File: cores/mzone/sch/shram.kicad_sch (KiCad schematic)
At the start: 10 parts

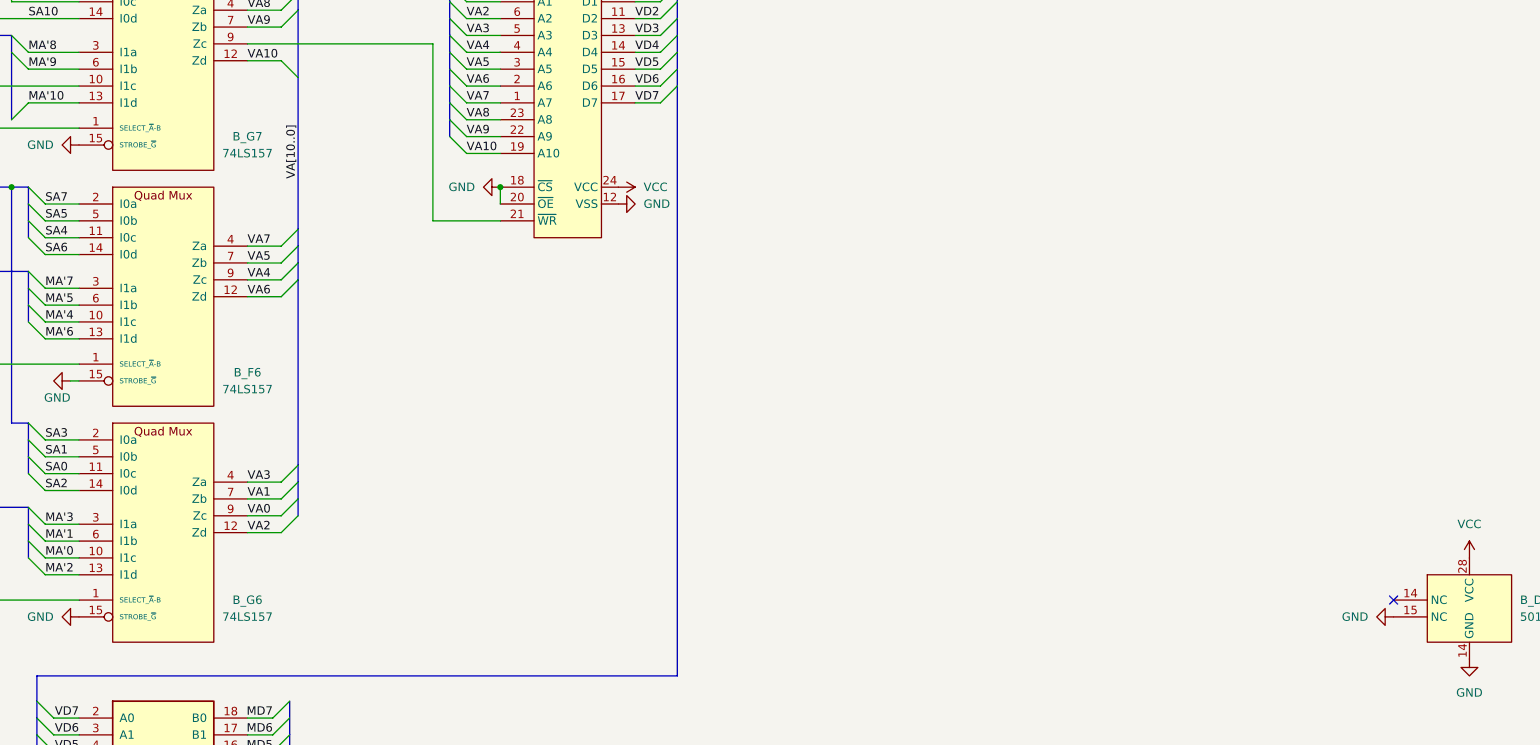
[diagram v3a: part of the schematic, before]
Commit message: mzone core
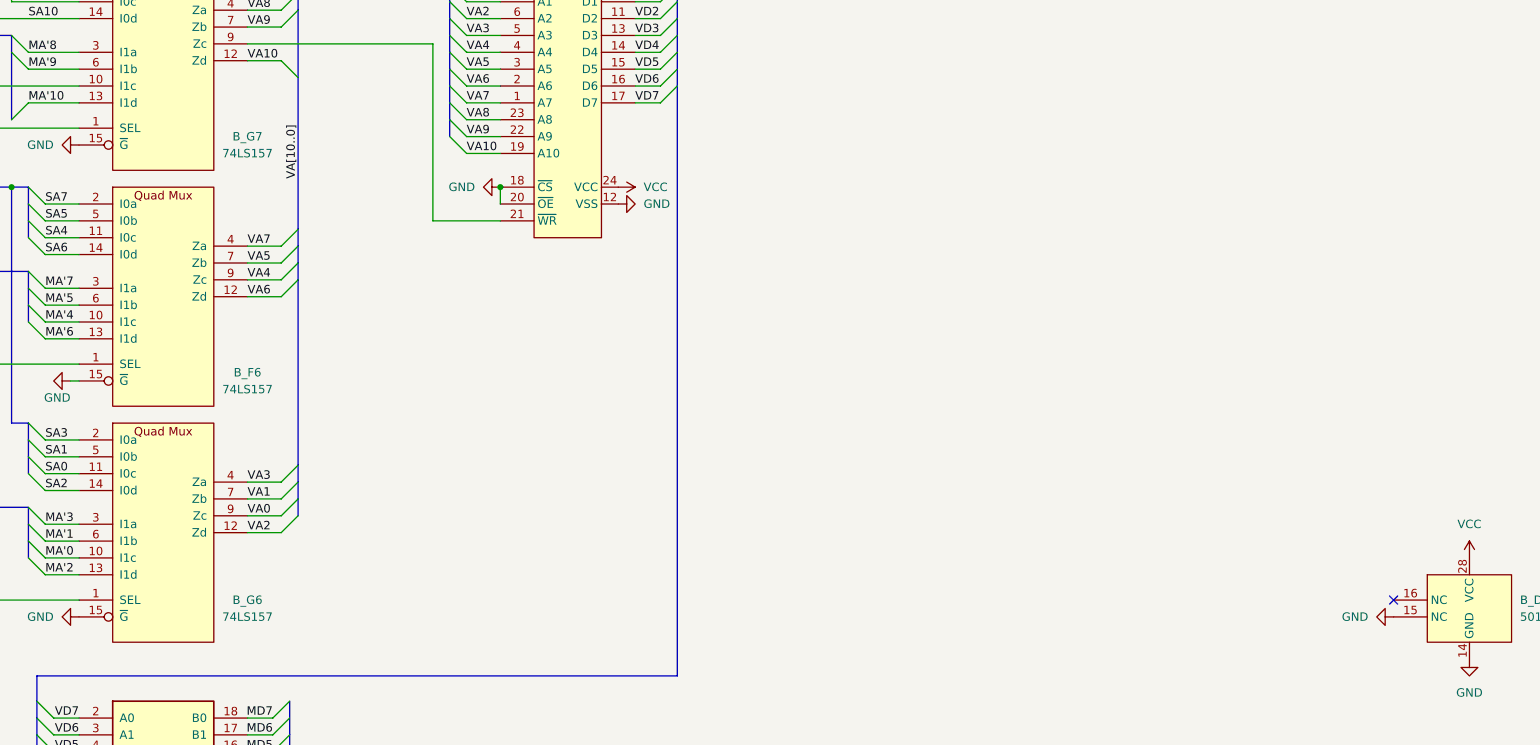
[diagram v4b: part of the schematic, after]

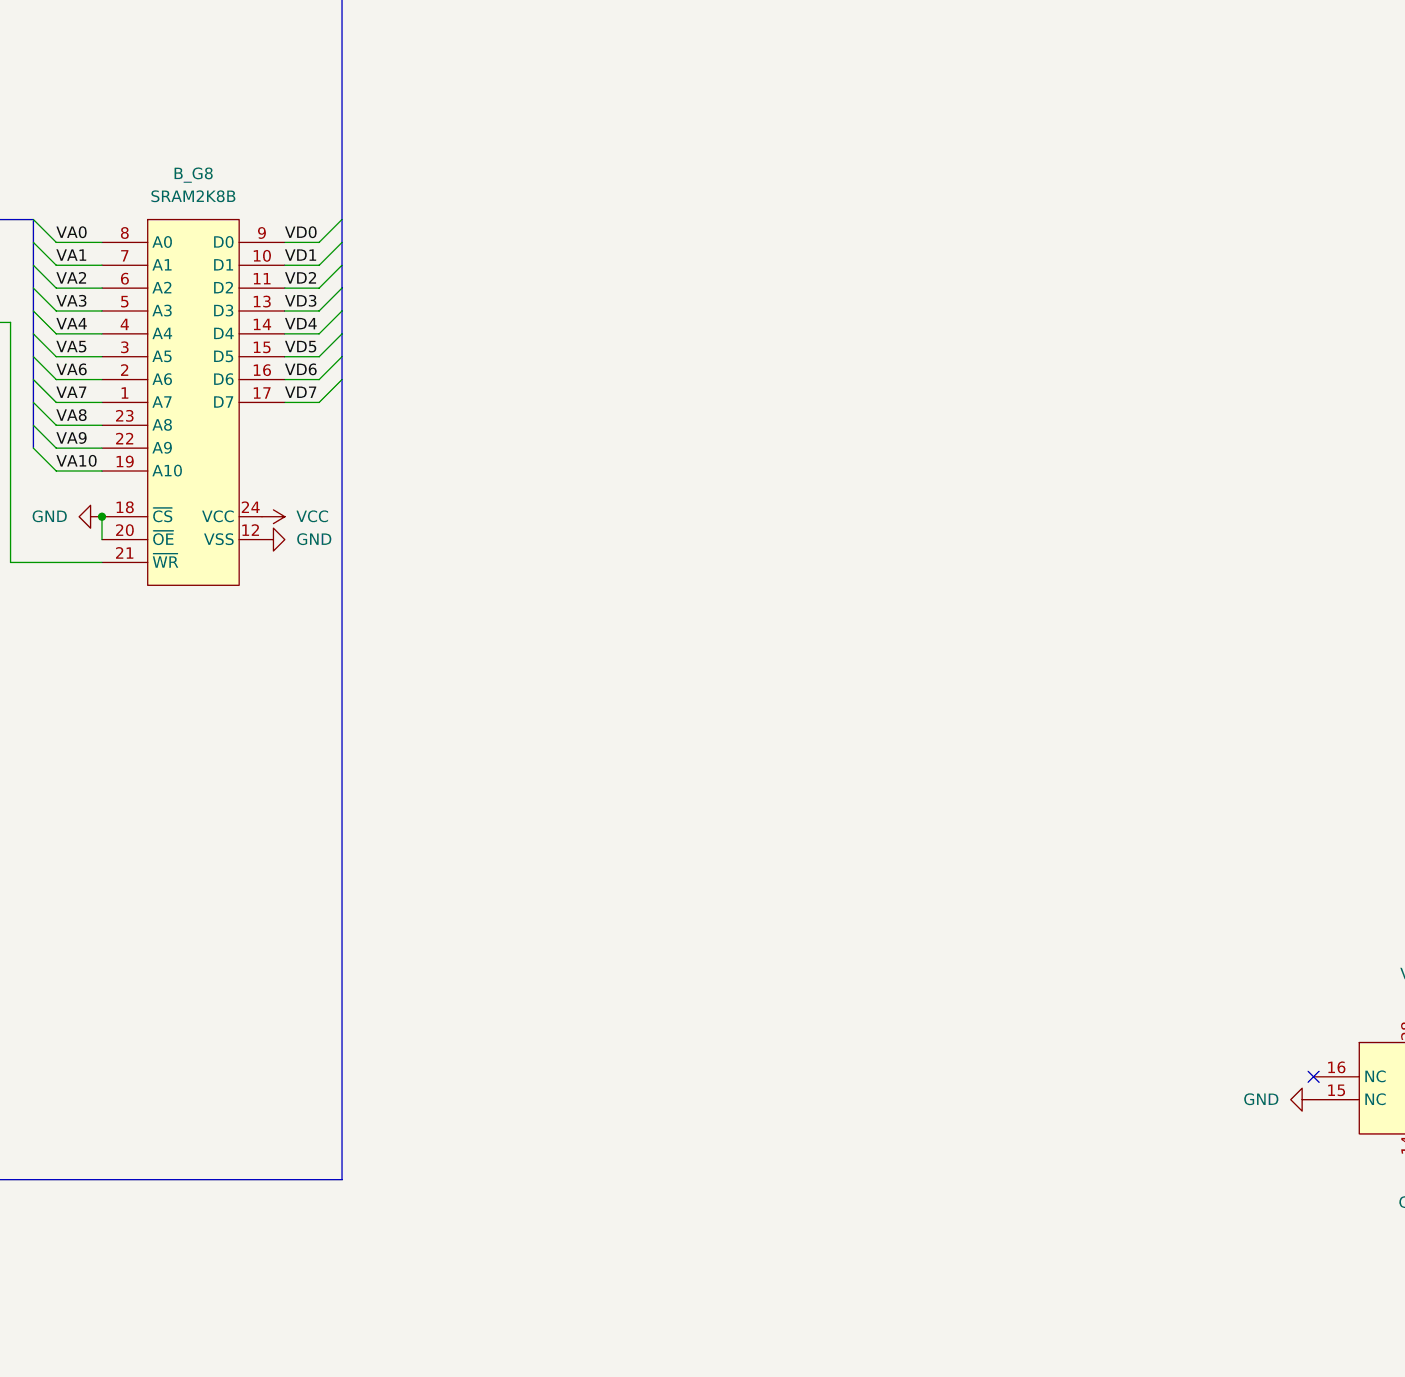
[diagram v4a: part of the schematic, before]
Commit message: mzone core
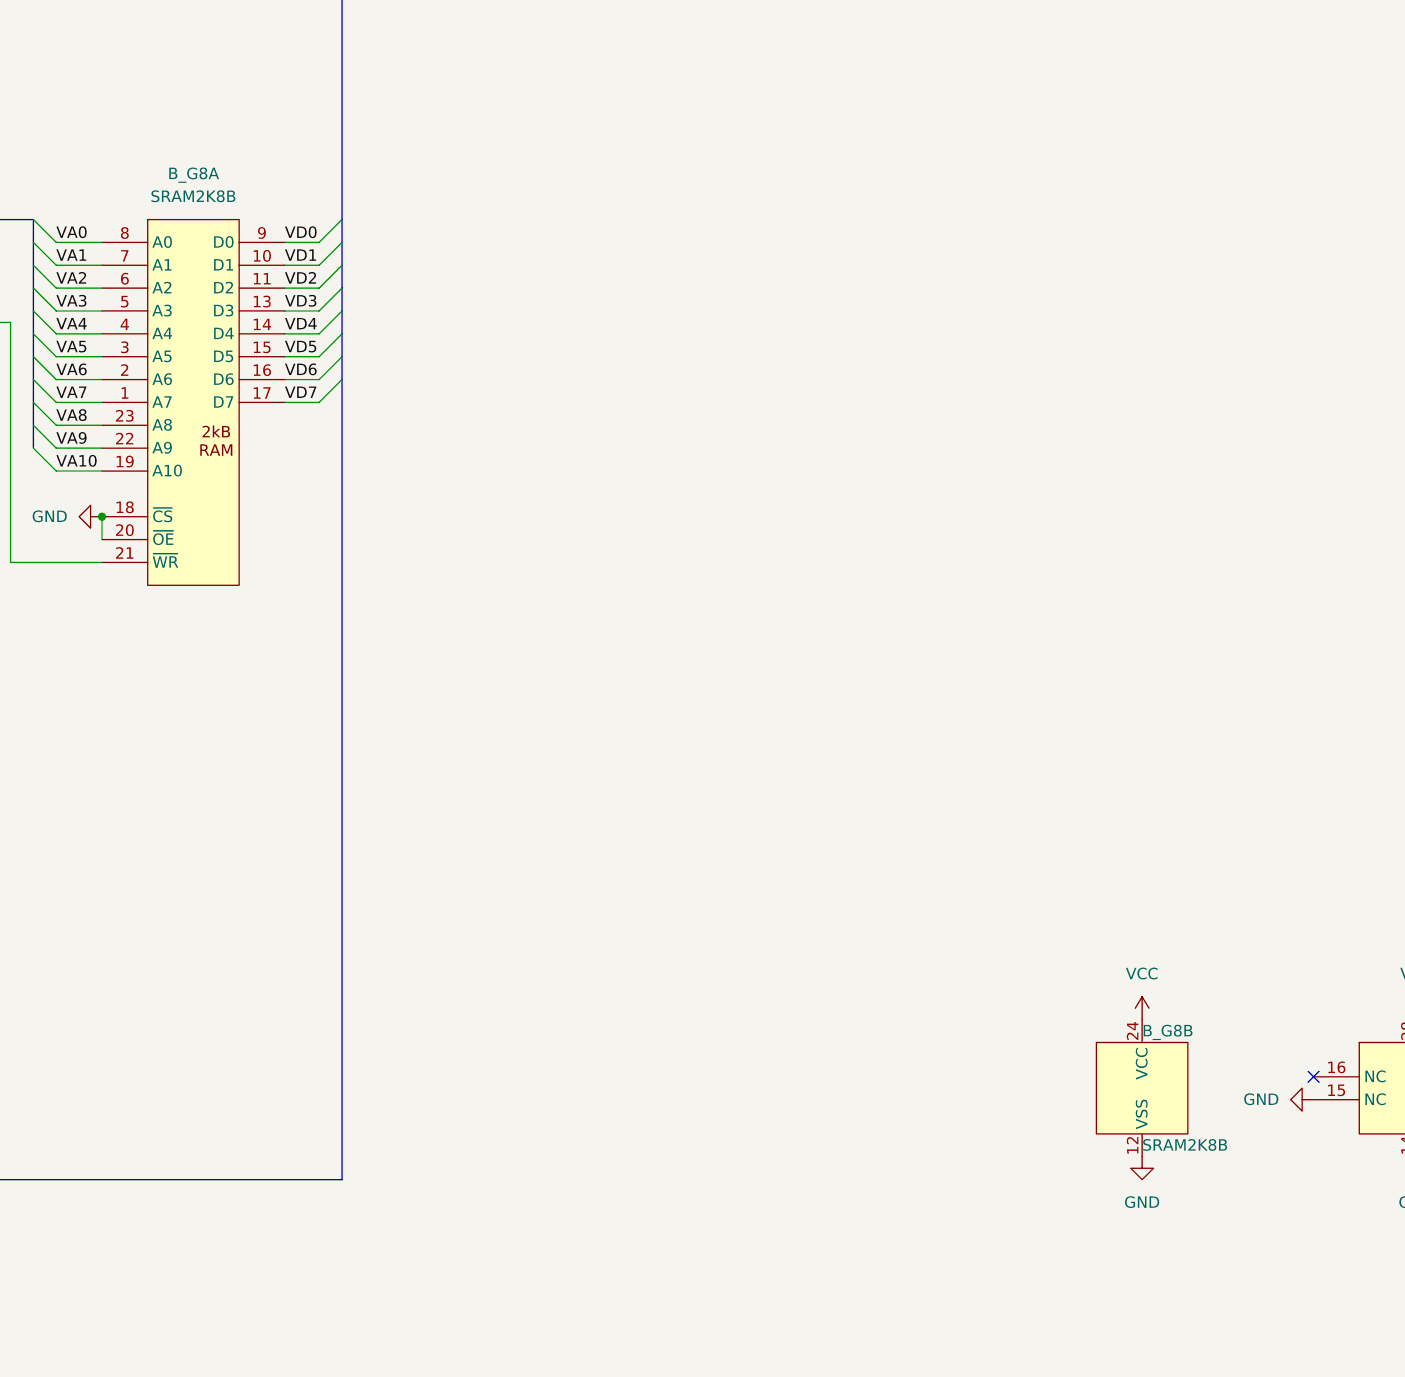
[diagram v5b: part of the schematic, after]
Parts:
- added unit 2 of B_G8
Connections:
- net GND: now also B_G8.12 (VSS); no longer B_G8.12 (VSS)
- net VCC: now also B_G8.24 (VCC); no longer B_G8.24 (VCC)

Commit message: mzone core
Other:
- company: (none) -> Konami GX319
- title: (none) -> Megazone
